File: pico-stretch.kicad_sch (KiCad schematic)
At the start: 62 parts, among them J1 Conn_01x32_MountingPin, J2 Conn_01x03_Pin, J3 Conn_01x32_MountingPin, U4 Winbond W25Q128JVSIQ, U5 RPI Radio Module 2, U6 ESP-PSRAM32

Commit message: Minor text update
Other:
- note added: "Adapted from an EasyEDA open source design: https://pro.easyeda.com/editor#id=a0a21c97b13d436db5579fc2a8b1625d and the Raspberry Pi Pico hardware design guide and reference designs. Part recommendations for the inductor, flash and clock crystal were followed."
- note added: "Pico Stretch RP2350B Devboard"
- note removed: "RP2350B"
- note removed: "The MCU page was adapted from an EasyEDA open source design: https://pro.easyeda.com/editor#id=a0a21c97b13d436db5579fc2a8b1625d Most significant modification was to use 'basic' components wherever possible. Part recommendations for the inductor, flash and clock crystal were followed."
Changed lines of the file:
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@@
 		)
 	)
-	(text "RP2350B"
+	(text "Pico Stretch RP2350B Devboard"
 		(exclude_from_sim no)
-		(at 126.238 32.004 0)
+		(at 57.658 28.448 0)
 		(effects
 			(font
@@
 		)
 	)
-	(text "The MCU page was adapted from an EasyEDA open source design:\nhttps://pro.easyeda.com/editor#id=a0a21c97b13d436db5579fc2a8b1625d\n\nMost significant modification was to use 'basic' components wherever possible.\n\nPart recommendations for the inductor, flash and clock crystal were followed."
+	(text "Adapted from an EasyEDA open source design:\nhttps://pro.easyeda.com/editor#id=a0a21c97b13d436db5579fc2a8b1625d and\nthe Raspberry Pi Pico hardware design guide and reference designs.\n\nPart recommendations for the inductor, flash and clock crystal were followed."
 		(exclude_from_sim no)
-		(at 127 57.15 0)
+		(at 102.616 51.308 0)
 		(effects
 			(font

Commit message: Fixes after review
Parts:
- added C21, C22, C23: 100nF, PCM_JLCPCB:C_0402, symbol PCM_JLCPCB-Capacitors:0402,100nF
- added C24: 4.7nF, PCM_JLCPCB:C_0603, symbol PCM_JLCPCB-Capacitors:0603,4.7nF
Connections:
- net 3V3: now also C21.1, C22.1, C23.1, C24.1
- net GND: now also C21.2, C22.2, C23.2, C24.2

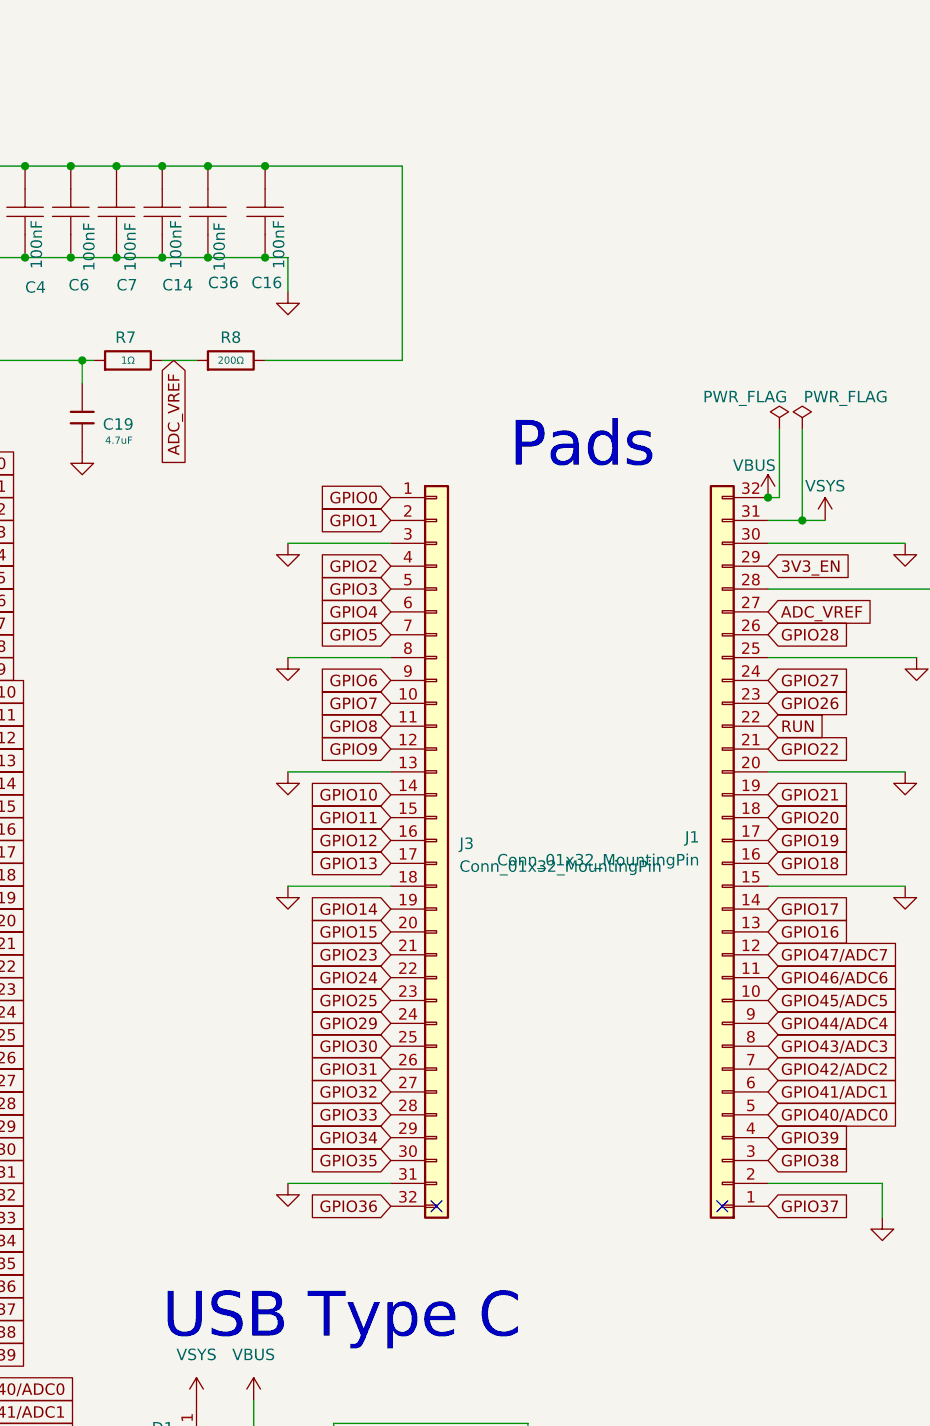
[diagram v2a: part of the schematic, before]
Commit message: Major re-work for castellated pads and PSRAM on top
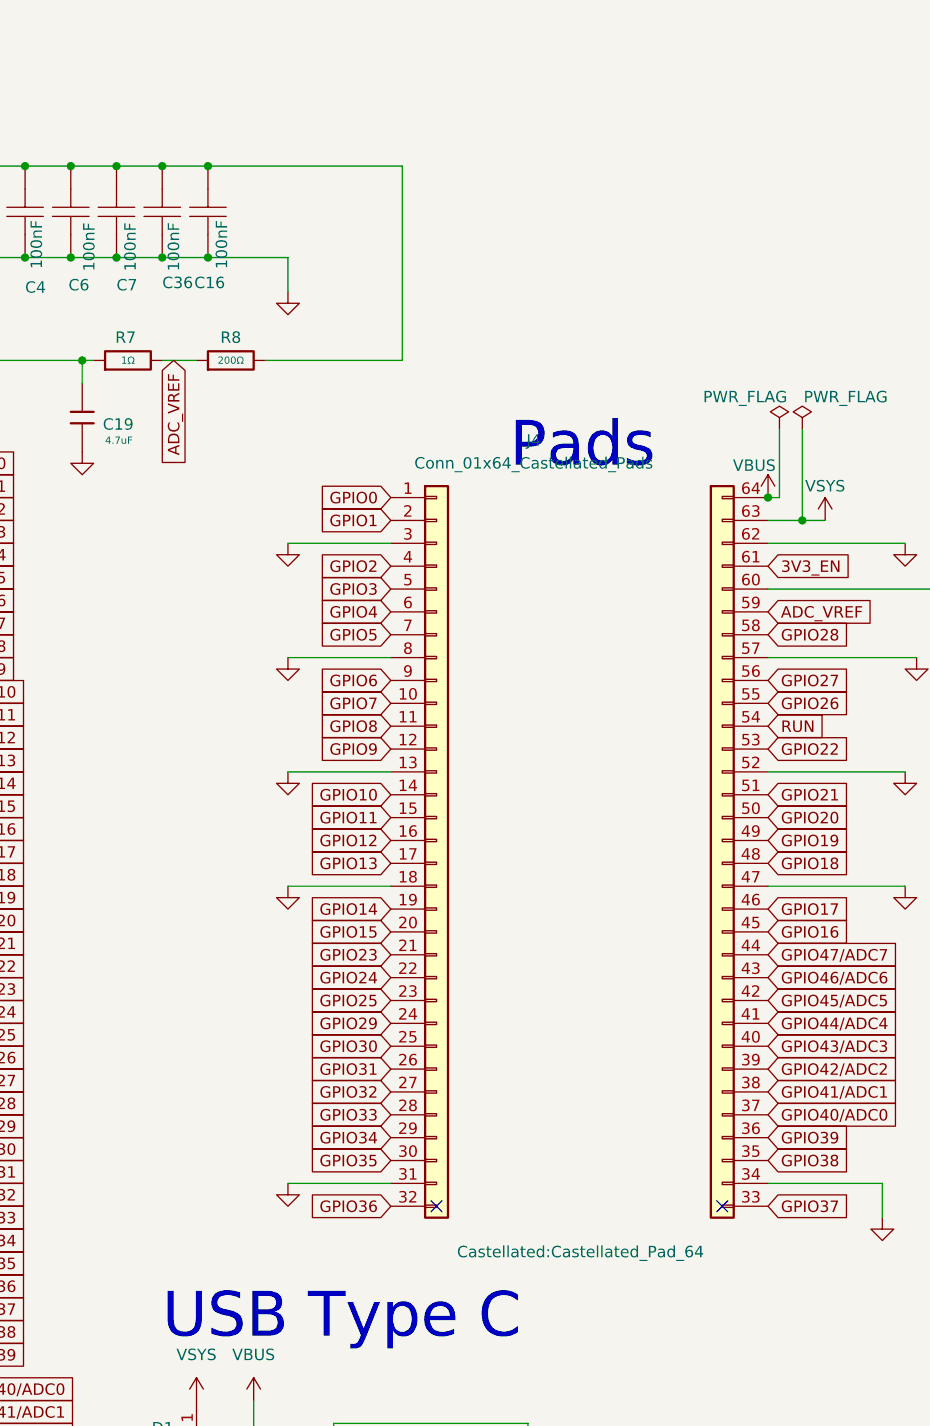
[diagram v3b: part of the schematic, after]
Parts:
- removed C14: 100nF, RP2350 Dev Board:C0402, symbol ProPrj_RP2-easyedapro:UMK105B7104KVHF
- removed J1: Conn_01x32_MountingPin, Custom:Pads_1x33_P2.54mm_Vertical_2, symbol Connector_Generic_MountingPin:Conn_01x32_MountingPin
- removed J3: Conn_01x32_MountingPin, Custom:Pads_1x33_P2.54mm_Vertical, symbol Connector_Generic_MountingPin:Conn_01x32_MountingPin
- added J4: Conn_01x64_Castellated_Pads, Castellated:Castellated_Pad_64, symbol Connector_Generic_MountingPin:Conn_01x64_Castellated_Pads
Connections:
- net 3V3: now also J4.60 (Pin_60)
- net 3V3_EN: now also J4.61 (Pin_61)
- net ADC_VREF: now also J4.59 (Pin_59)
- net GND: now also J4.13 (Pin_13), J4.18 (Pin_18), J4.3 (Pin_3), J4.31 (Pin_31), J4.34 (Pin_34), J4.47 (Pin_47), J4.52 (Pin_52), J4.57 (Pin_57), J4.62 (Pin_62), J4.8 (Pin_8)
- net GPIO0: now also J4.1 (Pin_1)
- net GPIO1: now also J4.2 (Pin_2)
- net GPIO10: now also J4.14 (Pin_14)
- net GPIO11: now also J4.15 (Pin_15)
- net GPIO12: now also J4.16 (Pin_16)
- net GPIO13: now also J4.17 (Pin_17)
- net GPIO14: now also J4.19 (Pin_19)
- net GPIO15: now also J4.20 (Pin_20)
- net GPIO16: now also J4.45 (Pin_45)
- net GPIO17: now also J4.46 (Pin_46)
- net GPIO18: now also J4.48 (Pin_48)
- net GPIO19: now also J4.49 (Pin_49)
- net GPIO2: now also J4.4 (Pin_4)
- net GPIO20: now also J4.50 (Pin_50)
- net GPIO21: now also J4.51 (Pin_61)
- net GPIO22: now also J4.53 (Pin_53)
- net GPIO23: now also J4.21 (Pin_21)
- net GPIO24: now also J4.22 (Pin_22)
- net GPIO25: now also J4.23 (Pin_23)
- net GPIO26: now also J4.55 (Pin_55)
- net GPIO27: now also J4.56 (Pin_56)
- net GPIO28: now also J4.58 (Pin_58)
- net GPIO29: now also J4.24 (Pin_24)
- net GPIO3: now also J4.5 (Pin_5)
- net GPIO30: now also J4.25 (Pin_25)
- net GPIO31: now also J4.26 (Pin_26)
- net GPIO32: now also J4.27 (Pin_27)
- net GPIO33: now also J4.28 (Pin_28)
- net GPIO34: now also J4.29 (Pin_29)
- net GPIO35: now also J4.30 (Pin_30)
- net GPIO36: now also J4.32 (Pin_32)
- net GPIO37: now also J4.33 (Pin_33)
- net GPIO38: now also J4.35 (Pin_35)
- net GPIO39: now also J4.36 (Pin_36)
- net GPIO4: now also J4.6 (Pin_6)
- net GPIO40/ADC0: now also J4.37 (Pin_37)
- net GPIO41/ADC1: now also J4.38 (Pin_38)
- net GPIO42/ADC2: now also J4.39 (Pin_39)
- net GPIO43/ADC3: now also J4.40 (Pin_40)
- net GPIO44/ADC4: now also J4.41 (Pin_41)
- net GPIO45/ADC5: now also J4.42 (Pin_42)
- net GPIO46/ADC6: now also J4.43 (Pin_43)
- net GPIO47/ADC7: now also J4.44 (Pin_44)
- net GPIO5: now also J4.7 (Pin_7)
- net GPIO6: now also J4.9 (Pin_9)
- net GPIO7: now also J4.10 (Pin_10)
- net GPIO8: now also J4.11 (Pin_11)
- net GPIO9: now also J4.12 (Pin_12)
- net RUN: now also J4.54 (Pin_54)
- net VBUS: now also J4.64 (Pin_64)
- net VSYS: now also J4.63 (Pin_63)
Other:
- moved on the sheet: C16, C36
